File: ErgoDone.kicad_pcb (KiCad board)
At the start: 2 copper layers, 182.8 x 158.9 mm, 152 parts, among them J1 USB, J2 3.5mm, J3 JMP, J4 JMP, SW0:10 SW0:3, SW0:11 SW0:2, SW0:12 SW0:1, SW0:7 SW0:6, SW0:8 SW0:5, SW0:9 SW0:4, SW1:10 SW1:3, SW1:11 SW1:2, SW1:12 SW1:1, SW1:13 SW1:0, SW1:9 SW1:4, SW2:10 SW2:3, SW2:11 SW2:2, SW2:12 SW2:1, SW2:13 SW2:0, SW2:7 SW2:6, SW2:8 SW2:5, SW2:9 SW2:4, SW3:10 SW3:3, SW3:11 SW3:2, SW3:12 SW3:1, SW3:13 SW3:0, SW3:8 SW3:5, SW3:9 SW3:4, SW4:10 SW4:3, SW4:11 SW4:2, SW4:12 SW4:1, SW4:13 SW4:0, SW4:7 SW4:6, SW4:8 SW4:5, SW4:9 SW4:4, SW5:10 SW5:3, SW5:11 SW5:2, SW5:12 SW5:1, SW5:13 SW5:0, SW5:7 SW5:6, SW5:8 SW5:5, SW5:9 SW5:4, U1 ProMicro, U2 MCP23017

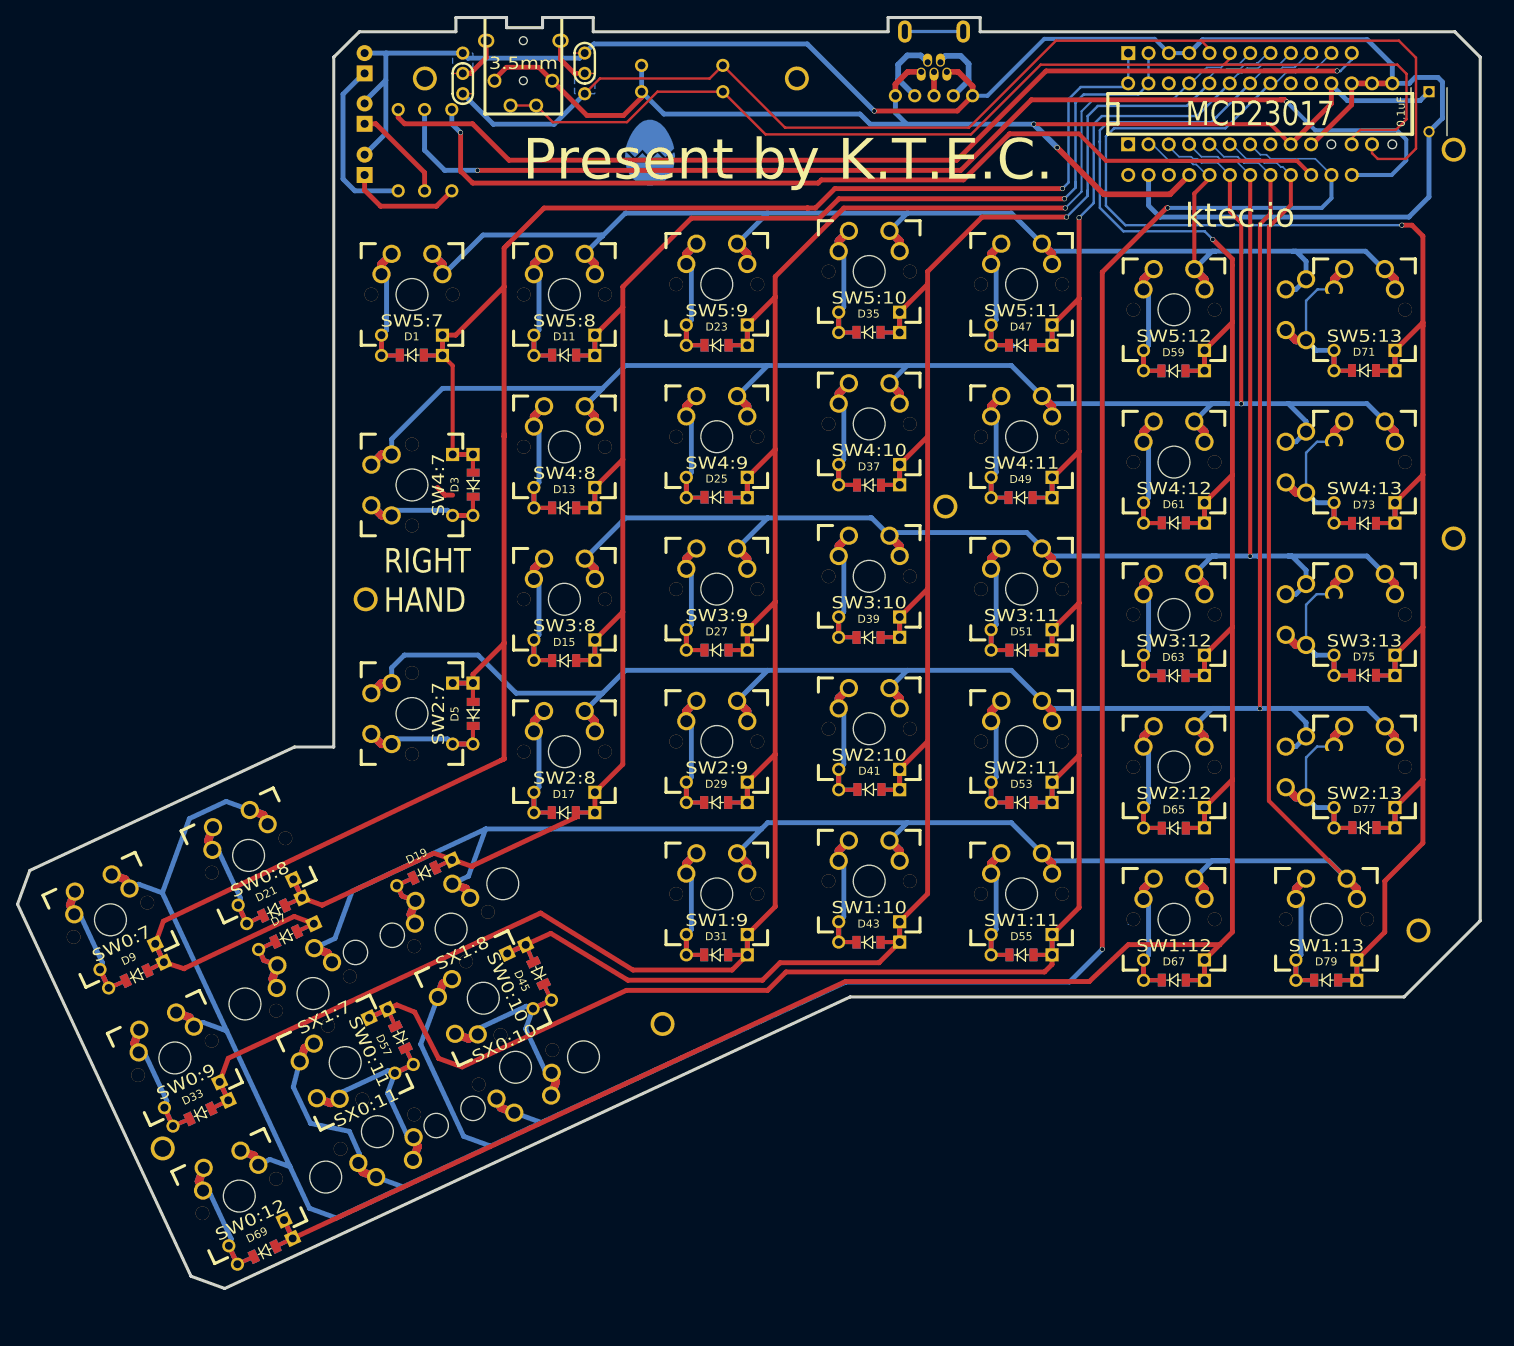
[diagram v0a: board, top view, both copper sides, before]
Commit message: what
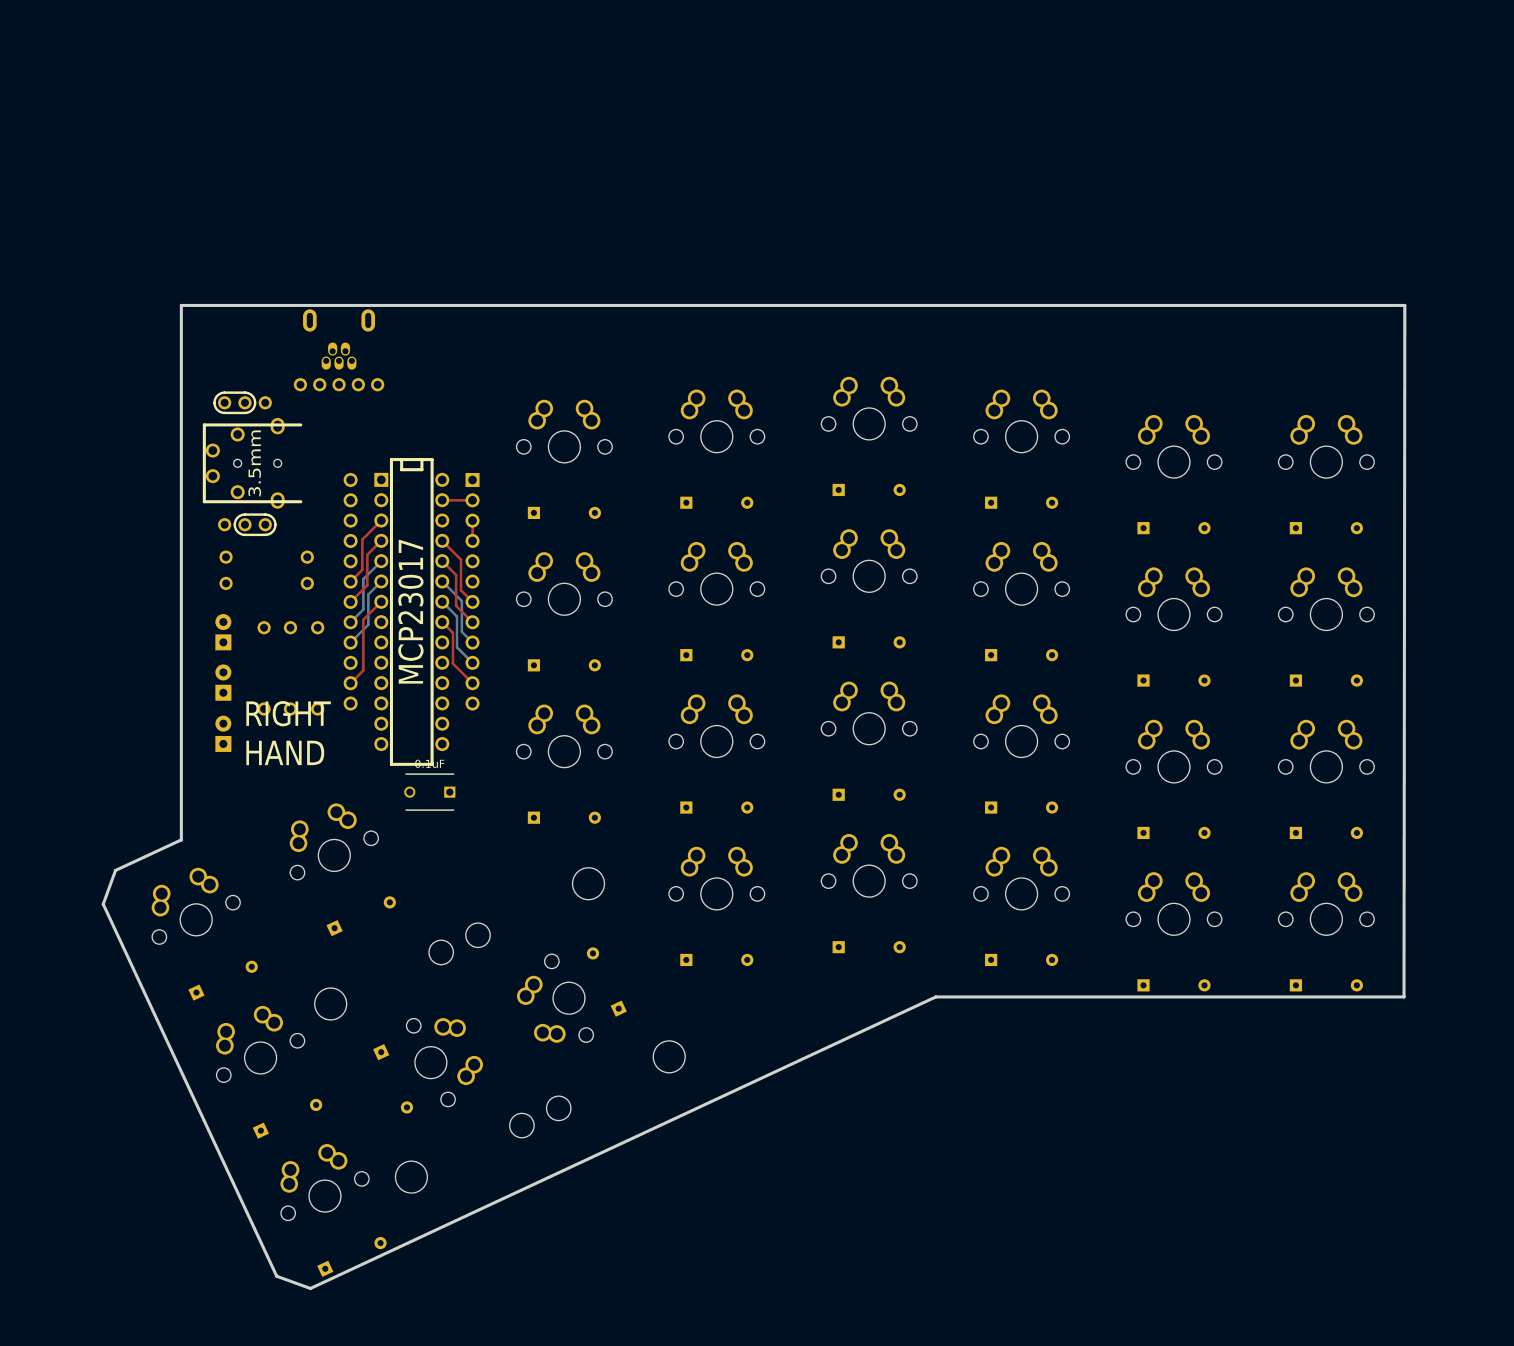
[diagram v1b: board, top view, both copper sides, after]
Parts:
- removed D1, D11, D13, D15, D17, D19, D21, D23, D25, D27, D29, D3, D31, D33, D35, D37, D39, D41, D43, D45, D47, D49, D5, D51, D53, D55, D57, D59, D61, D63, D65, D67, D69, D7, D71, D73, D75, D77, D79, D9: DIODE, ErgoDone:D_1206_L
- removed D10, D12, D14, D16, D18, D2, D20, D22, D24, D26, D28, D30, D32, D34, D36, D38, D4, D40, D42, D44, D46, D48, D50, D52, D54, D56, D58, D6, D60, D62, D64, D66, D68, D70, D72, D74, D76, D78, D8, D80: DIODE, ErgoDone:D_1206_R
- removed D81, D82: DIODE, ErgoDone:DIODE_SX
- removed G*** (x2): LOGO, ErgoDox_pro_micro_edition:ergo_icon
- removed REF** (x9): hole_r1.75, YD_modules:hole_r1.75
- removed S1, S2: STAB200, ErgoDone:STAB_PCB940
- removed SW0:7: SW0:6, ErgoDone:MX_FLIP_DIODE_NOSMD
- removed SW2:7: SW2:6, ErgoDone:MX_FLIP_DIODE_NOSMD
- removed SW4:7: SW4:6, ErgoDone:MX_FLIP_DIODE_NOSMD
- removed SW5:10: SW5:3, ErgoDone:MX_FLIP_DIODE_NOSMD
- removed SW5:11: SW5:2, ErgoDone:MX_FLIP_DIODE_NOSMD
- removed SW5:12: SW5:1, ErgoDone:MX_FLIP_DIODE_NOSMD
- removed SW5:13: SW5:0, ErgoDone:MX_FLIP_XX_NOSMD
- removed SW5:7: SW5:6, ErgoDone:MX_FLIP_DIODE_NOSMD
- removed SW5:8: SW5:5, ErgoDone:MX_FLIP_DIODE_NOSMD
- removed SW5:9: SW5:4, ErgoDone:MX_FLIP_DIODE_NOSMD
- removed SX0:10: SX0:3, ErgoDone:MX_FLIP
- removed SX0:11: SX0:2, ErgoDone:MX_FLIP
- removed SX1:7: SX1:6, ErgoDone:MX_FLIP
- SW0:10, SW0:11: footprint ErgoDone:MX_FLIP_DIODE_NOSMD -> ErgoDone:200-dual
- SW0:12, SW0:8, SW0:9, SW1:10, SW1:11, SW1:12, SW1:13, SW1:9, SW2:10, SW2:11, SW2:12, SW2:8, SW2:9, SW3:10, SW3:11, SW3:12, SW3:8, SW3:9, SW4:10, SW4:11, SW4:12, SW4:8, SW4:9: footprint ErgoDone:MX_FLIP_DIODE_NOSMD -> ErgoDone:100-dual
- SW2:13, SW3:13, SW4:13: footprint ErgoDone:MX_FLIP_XX_NOSMD -> ErgoDone:100-dual
- SX1:8: footprint ErgoDone:MX_FLIP -> ErgoDone:100-dual
- moved C1 150.5 mm to (77.1, 127.3), turned to 180 degrees
- moved U2 123.0 mm to (72.4, 104.8), turned to 270 degrees
- moved U1 119.5 mm to (72.3, 102.3), turned to 270 degrees
- moved J1 82.7 mm to (63.3, 66.6)
- moved R1 80.5 mm to (54.2, 97.9)
- moved R2 80.5 mm to (54.2, 101.2)
- moved LED_B1 73.3 mm to (48.8, 114.9)
- moved LED_C1 73.3 mm to (48.8, 121.3)
- moved LED_A1 73.3 mm to (48.8, 108.6)
- moved J3 70.6 mm to (51.5, 93.9), turned to 0 degrees
- moved RA1 66.9 mm to (53.9, 111.8)
- moved RB1 66.9 mm to (57.2, 111.8)
- moved RC1 66.9 mm to (60.6, 111.8)
- moved J2 62.3 mm to (58.5, 86.2), turned to 180 degrees
- moved J4 49.4 mm to (51.5, 78.6), turned to 0 degrees
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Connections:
- C1 pad 1: VCC -> (no net)
- C1 pad 2: GND -> (no net)
- SX1:8 pad 2: Net-(D19-Pad1) -> Net-(SX1:8-Pad2)
- U1 pad 1: /COL6 -> (no net)
- U1 pad 25: /ROW5 -> (no net)
- U2 pad 2: /ROW5 -> (no net)
- U2 pad 28: /COL6 -> (no net)
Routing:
- net /ROW0: track 411.9 -> 11.8 mm, vias 2 -> 0
- net /COL1: track 352.0 -> 9.20 mm, vias 1 -> 0
- net /COL6: track 305.4 -> 0.00 mm, vias 1 -> 0
- net /COL4: track 314.3 -> 9.20 mm, vias 1 -> 0
- net /ROW1: track 306.2 -> 9.22 mm
- net /COL11: track 302.0 -> 9.20 mm, vias 1 -> 0
- net /ROW2: track 277.7 -> 9.22 mm, vias 1 -> 0
- net /COL10: track 273.7 -> 9.20 mm, vias 1 -> 0
- net /COL5: track 256.2 -> 3.79 mm, vias 1 -> 0
- net GND: track 243.0 -> 2.54 mm, vias 1 -> 0
- net /COL0: track 246.3 -> 9.20 mm, vias 1 -> 0
- net /ROW4: track 241.6 -> 9.22 mm, vias 1 -> 0
- net /ROW5: track 211.8 -> 0.00 mm
- net /ROW3: track 217.6 -> 9.22 mm, vias 1 -> 0
- net VCC: track 168.7 -> 0.00 mm, vias 2 -> 0
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- removed copper zone on B.Cu, net (none)
- removed copper zone on F.Cu, net (none)
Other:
- board size 182.8 x 158.9 mm -> 162.7 x 122.9 mm
- board text removed: "+"
- board text removed: "-"
- board text removed: "5V"
- board text removed: "D+"
- board text removed: "D-"
- board text removed: "ErgoD ne"
- board text removed: "GND"
- board text removed: "ID"
- board text removed: "Present by K.T.E.C."
- board text removed: "USB"
- board text removed: "Ver 1.5"
- board text removed: "ktec.io"

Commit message: whatever
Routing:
- net /COL1: track 9.20 -> 379.0 mm
- net /COL11: track 9.20 -> 306.9 mm, vias 0 -> 1
- net /COL0: track 9.20 -> 262.8 mm
- net /COL4: track 9.20 -> 240.5 mm
- net /COL10: track 9.20 -> 232.3 mm, vias 0 -> 1
- net /ROW2: track 9.22 -> 228.7 mm
- net /ROW1: track 9.22 -> 207.5 mm
- net /ROW3: track 9.22 -> 206.6 mm
- net /ROW4: track 9.22 -> 177.2 mm
- net /COL5: track 3.79 -> 152.9 mm
- net /ROW0: track 11.8 -> 103.1 mm
- net GND: track 2.54 -> 72.2 mm, vias 0 -> 1
- net /SDAM: track 0.00 -> 59.9 mm
- net VCC: track 0.00 -> 59.0 mm
- net /SCLM: track 0.00 -> 31.1 mm
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- added copper zone on B.Cu, net GND
- added copper zone on F.Cu, net GND
